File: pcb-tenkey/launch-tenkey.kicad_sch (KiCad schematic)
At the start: 64 parts, among them J7 FH12-16S-0.5SH(55)

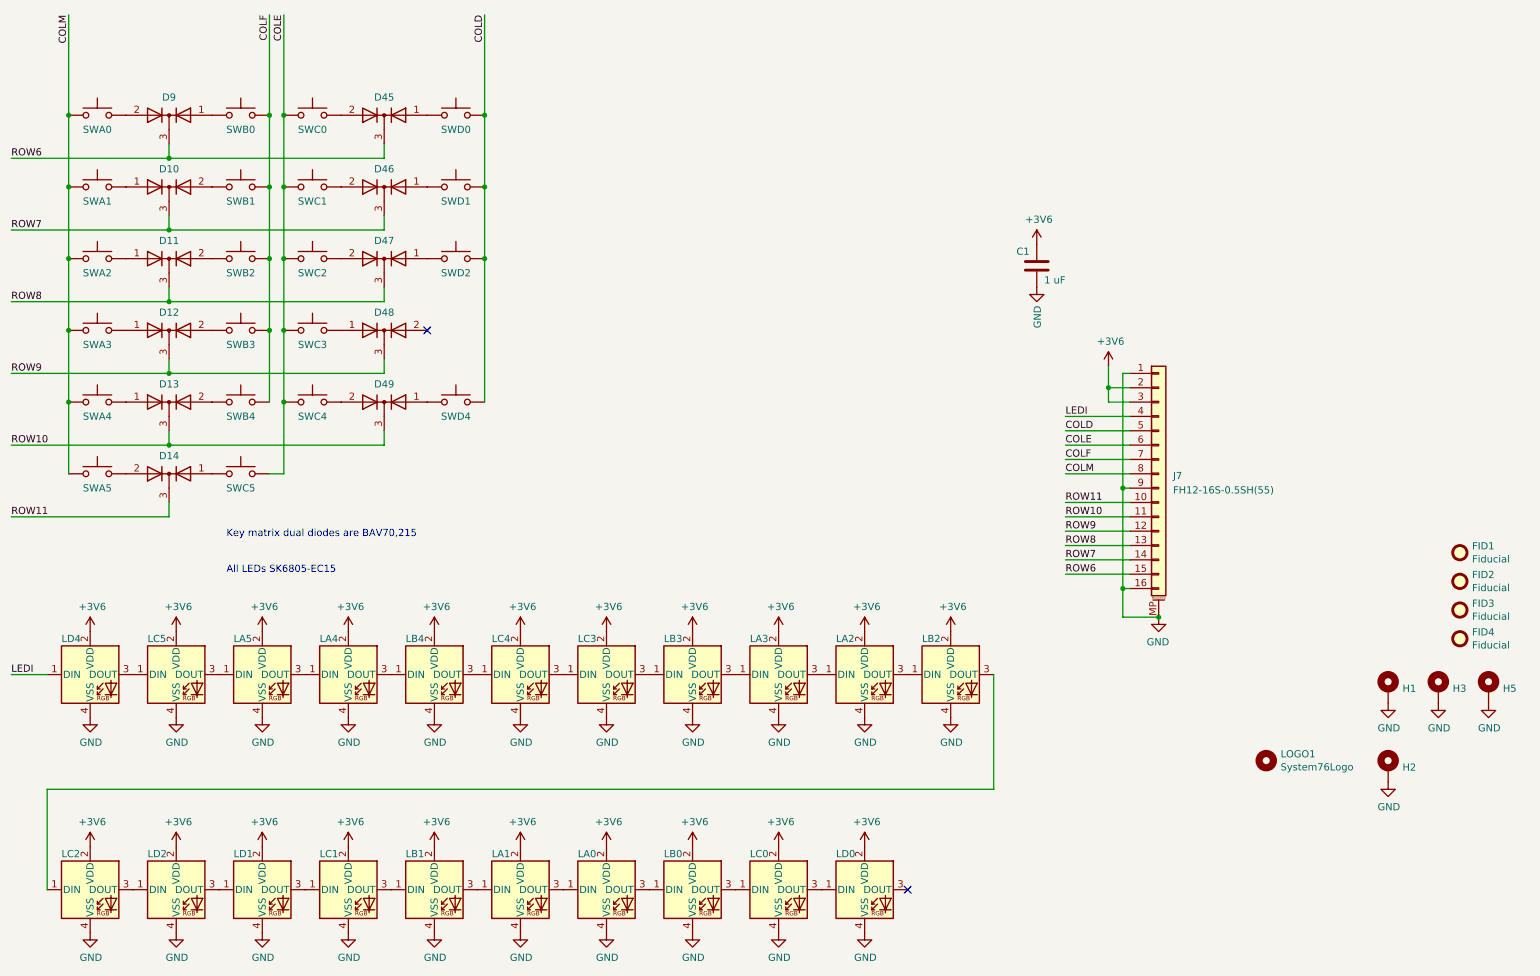
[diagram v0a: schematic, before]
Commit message: version pins, finalize routing FFC connector changed to 20 pin USB hub reset pull down via stitching route remaining nets and cleanup
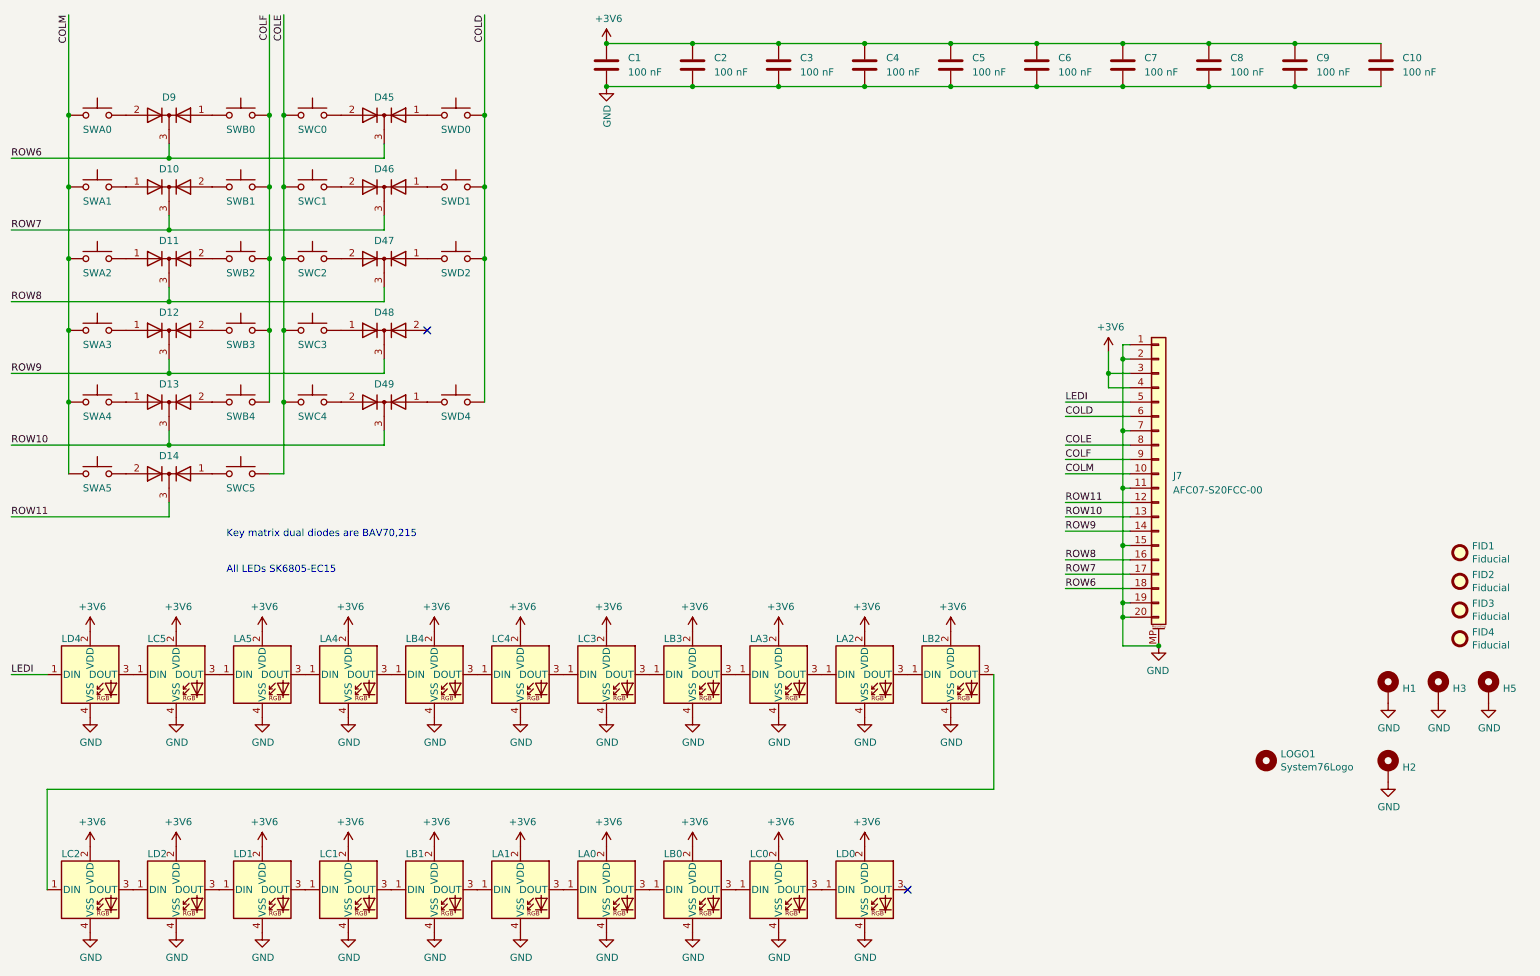
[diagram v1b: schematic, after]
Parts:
- added C10, C2, C3, C4, C5, C6, C7, C8, C9: 100 nF, Capacitor_SMD:C_0603_1608Metric, symbol Device:C
- C1: value 1 uF -> 100 nF
- J7: value FH12-16S-0.5SH(55) -> AFC07-S20FCC-00; footprint Connector_FFC-FPC:Hirose_FH12-16S-0.5SH_1x16-1MP_P0.50mm_Horizontal -> launch:AFC07-S20FCC-00; symbol Connector_Generic_MountingPin:Conn_01x16_MountingPin -> Connector_Generic_MountingPin:Conn_01x20_MountingPin
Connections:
- net +3V6: now also J7.4 (Pin_4), C10.2, C2.2, C3.2, C4.2, C5.2, C6.2, C7.2, C8.2, C9.2; no longer J7.2 (Pin_2)
- net COLD: now also J7.6 (Pin_6); no longer J7.5 (Pin_5)
- net COLE: now also J7.8 (Pin_8); no longer J7.6 (Pin_6)
- net COLF: now also J7.9 (Pin_9); no longer J7.7 (Pin_7)
- net COLM: now also J7.10 (Pin_10); no longer J7.8 (Pin_8)
- net GND: now also J7.11 (Pin_11), J7.15 (Pin_15), J7.19 (Pin_19), J7.2 (Pin_2), J7.20 (Pin_20), J7.7 (Pin_7), C10.1, C2.1, C3.1, C4.1, C5.1, C6.1, C7.1, C8.1, C9.1; no longer J7.16 (Pin_16), J7.9 (Pin_9)
- net LEDI: now also J7.5 (Pin_5); no longer J7.4 (Pin_4)
- net ROW10: now also J7.13 (Pin_13); no longer J7.11 (Pin_11)
- net ROW11: now also J7.12 (Pin_12); no longer J7.10 (Pin_10)
- net ROW6: now also J7.18 (Pin_18); no longer J7.15 (Pin_15)
- net ROW7: now also J7.17 (Pin_17); no longer J7.14 (Pin_14)
- net ROW8: now also J7.16 (Pin_16); no longer J7.13 (Pin_13)
- net ROW9: now also J7.14 (Pin_14); no longer J7.12 (Pin_12)
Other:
- moved on the sheet: C1
